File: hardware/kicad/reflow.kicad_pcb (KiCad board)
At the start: 2 copper layers, 104 x 104 mm, 35 parts, among them J1 2 pol skrueterminal, J2 2 pol skrueterminal, J3 MAX31855, J4 OLED, Q1 IRFS4710, Q2 BS170, Q3 BS170, SW1 Rotary 1x12 EYE, SW2 Pushbutton, U2 LM2575-ADJ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

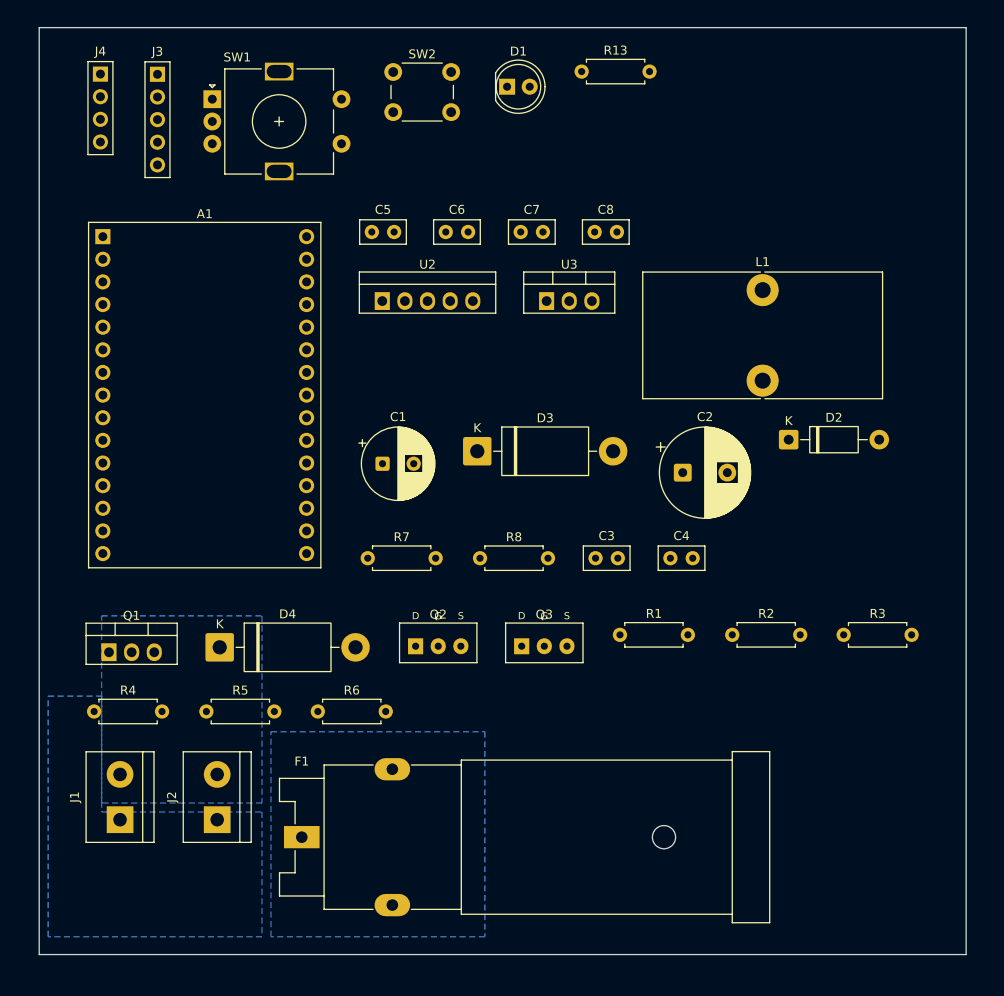
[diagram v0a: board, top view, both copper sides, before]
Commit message: hardware: two-stage route (165 B.Cu tracks + 86 F.Cu jumper segs); 4 connections need manual finish
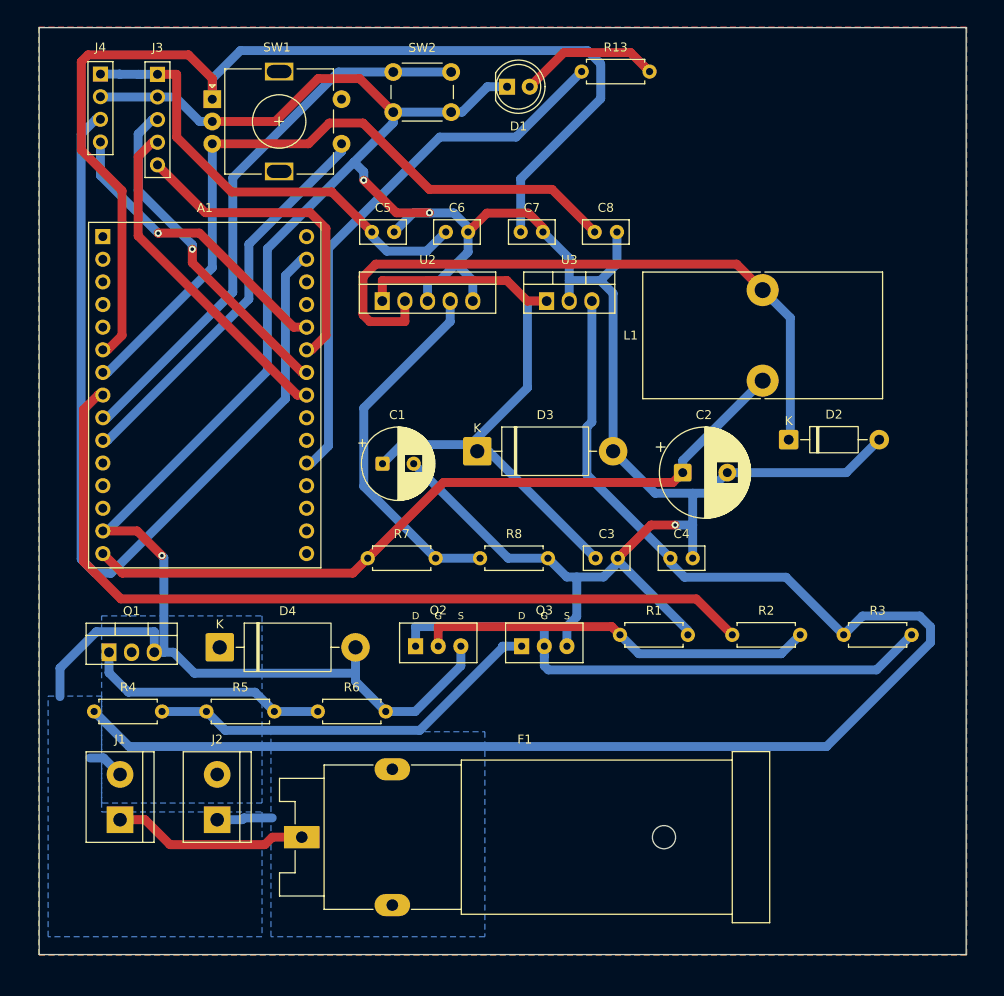
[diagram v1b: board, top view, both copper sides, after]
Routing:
- net /GND: track 0.00 -> 384.5 mm, vias 0 -> 4
- net /+12V: track 0.00 -> 169.5 mm
- net /GPIO32: track 0.00 -> 124.2 mm
- net /GPIO22: track 0.00 -> 99.2 mm
- net /GPIO25: track 0.00 -> 96.1 mm
- net /+5V: track 0.00 -> 84.7 mm
- net /GPIO33: track 0.00 -> 80.0 mm
- net /+24V: track 0.00 -> 78.9 mm
- net /SW_OUT: track 0.00 -> 76.4 mm
- net /GD_NODE1: track 0.00 -> 64.1 mm
- net /GPIO26: track 0.00 -> 62.7 mm
- net /GPIO4: track 0.00 -> 62.0 mm
- net /+3V3: track 0.00 -> 52.3 mm
- net /GATE_MAIN: track 0.00 -> 45.2 mm
- net /Q2_GATE: track 0.00 -> 44.9 mm
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- added copper zone on B.Cu, net (none)
- added copper zone on F.Cu, net (none)
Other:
- board text added: "A1"
- board text added: "C1"
- board text added: "C2"
- board text added: "C3"
- board text added: "C4"
- board text added: "C5"
- board text added: "C6"
- board text added: "C7"
- board text added: "C8"
- board text added: "D1"
- board text added: "D2"
- board text added: "D3"
- board text added: "D4"
- board text added: "F1"
- board text added: "J1"
- board text added: "J2"
- board text added: "J3"
- board text added: "J4"
- board text added: "L1"
- board text added: "Q1"
- board text added: "Q2"
- board text added: "Q3"
- board text added: "R1"
- board text added: "R13"
- board text added: "R2"
- board text added: "R3"
- board text added: "R4"
- board text added: "R5"
- board text added: "R6"
- board text added: "R7"
- board text added: "R8"
- board text added: "SW1"
- board text added: "SW2"
- board text added: "U2"
- board text added: "U3"

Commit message: hardware: close +3V3 on B.Cu; +24V/HEATER_RET need wire bridges
Route A1.30 (/+3V3) to the +3V3 net with a 6-segment B.Cu track down the
clear lane between the ESP module pin column and the buck input, landing on
the existing +3V3 copper. Refill zones. DRC: 0 copper-rule violations, +3V3
connected.

The two high-current crossings (+24V buck-input rail to its pour/F1.2, and
HEATER_RET upper pads to the lower pour island) cannot be closed on the
single-sided B.Cu copper: exhaustive search finds no path at the 1.0 mm
minimum track and no fillable pour neck down to 0.3 mm, because the
buck/gate-drive band plus the full-width +12V track form a continuous
clearance fence. They are left for a manual top-side wire bridge sized for
13 A (HEATER_RET clears at 2.0 mm; +24V at 1.0 mm or with a small
re-placement), rather than forcing a thin power jumper.

Pours intact; board still single-sided (no new B.Cu/F.Cu copper).
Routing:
- net /+3V3: track 52.3 -> 93.0 mm
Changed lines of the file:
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@@
+	)
+	(segment
+		(start 56 45.08)
+		(end 60.5 45.08)
+		(width 1)
+		(layer "B.Cu")
+		(net "/+3V3")
 	)
 	(segment
@@
 	)
 	(segment
+		(start 54.5 66)
+		(end 54.5 54.5)
+		(width 1)
+		(layer "B.Cu")
+		(net "/+3V3")
+	)
+	(segment
+		(start 54.5 54.5)
+		(end 54.5 46)
+		(width 1)
+		(layer "B.Cu")
+		(net "/+3V3")
+	)
+	(segment
 		(start 57.32 43.4026)
 		(end 57.32 42.93)
+		(width 1)
+		(layer "B.Cu")
+		(net "/+3V3")
+	)
+	(segment
+		(start 52 78)
+		(end 54.5 66)
 		(width 1)
 		(layer "B.Cu")
@@
 		(width 1)
 		(layer "B.Cu")
+		(net "/+3V3")
+	)
+	(segment
+		(start 54.5 46)
+		(end 56 45.08)
+		(width 1)
+		(layer "B.Cu")
+		(net "/+3V3")
+	)
+	(segment
+		(start 50 79.01)
+		(end 52 78)
+		(width 1)
+		(layer "B.Cu")

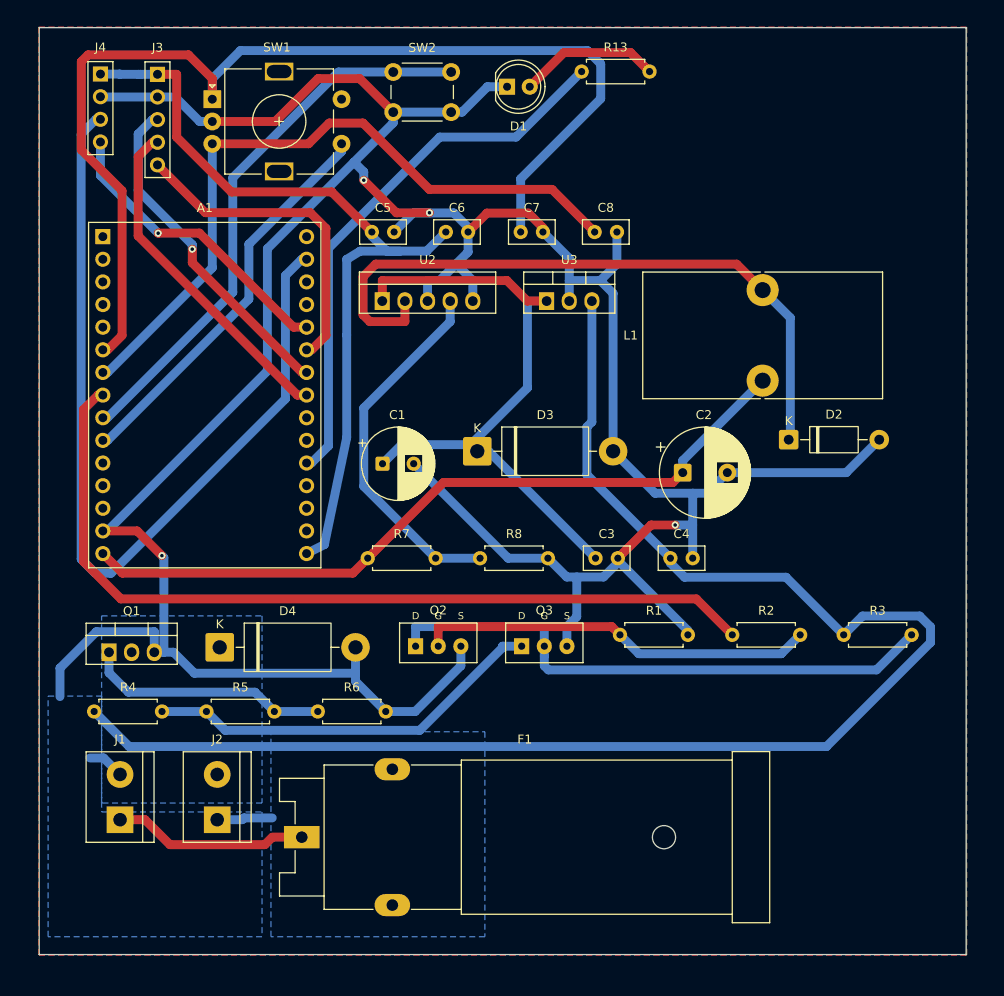
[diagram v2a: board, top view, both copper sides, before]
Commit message: hardware: update board with re-placed footprints (user re-placement)
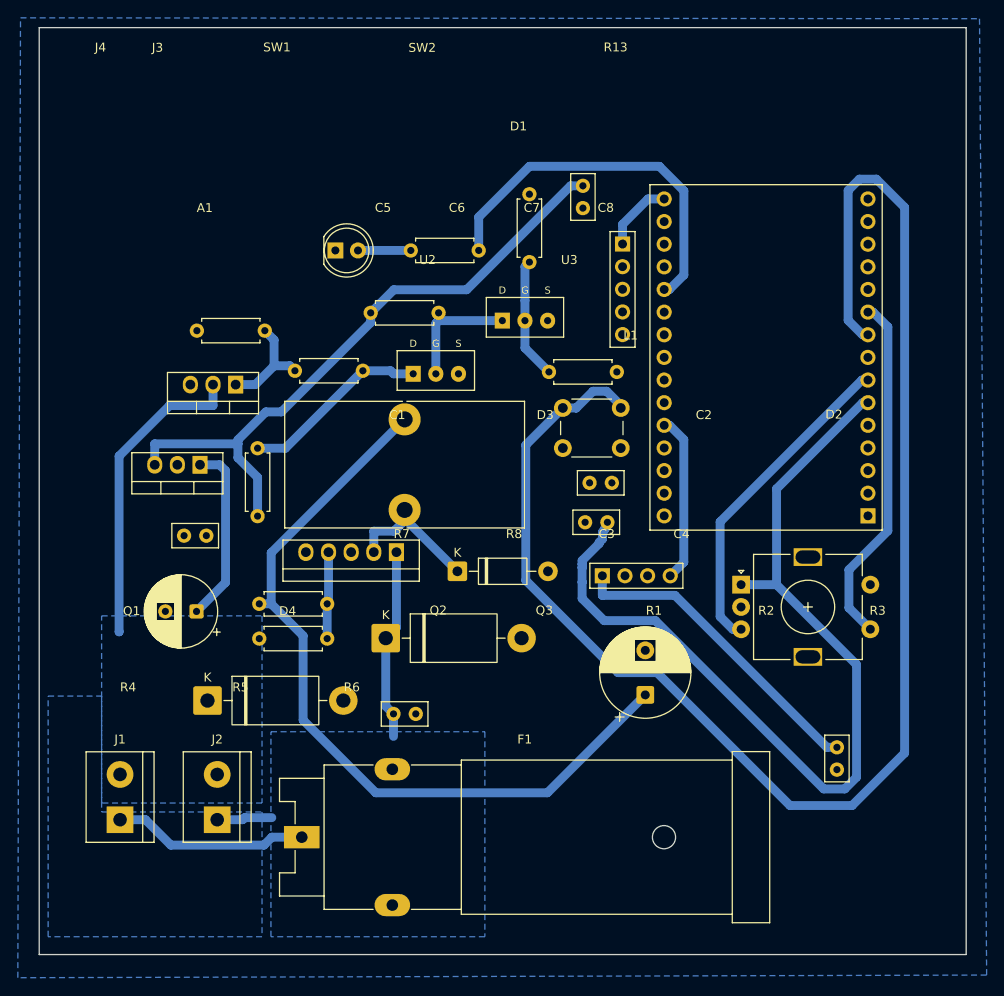
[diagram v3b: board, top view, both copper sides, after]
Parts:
- moved A1 91.4 mm to (113.0, 74.8), turned to 180 degrees
- moved SW1 80.5 mm to (98.8, 82.5)
- moved J4 79.6 mm to (83.2, 81.5), turned to 90 degrees
- moved C5 77.9 mm to (109.5, 100.8), turned to -90 degrees
- moved R3 64.2 mm to (57.2, 52.0)
- moved J3 55.5 mm to (85.5, 44.3)
- moved L1 47.1 mm to (61.0, 74.1), turned to 180 degrees
- moved C6 43.4 mm to (38.8, 77.0), turned to 180 degrees
- moved R6 43.1 mm to (45.3, 54.0), turned to 180 degrees
- moved R1 43.0 mm to (75.0, 46.3), turned to 90 degrees
- moved U3 43.0 mm to (38.0, 69.0), turned to 180 degrees
- moved C4 42.9 mm to (81.0, 37.8), turned to -90 degrees
- moved SW2 42.2 mm to (78.8, 62.7)
- moved R5 42.1 mm to (56.3, 58.5), turned to 180 degrees
- moved D2 40.0 mm to (66.9, 81.0)
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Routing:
- net /GND: track 384.5 -> 0.00 mm, vias 4 -> 0
- net /GPIO26: track 62.7 -> 171.6 mm
- net /GPIO22: track 99.2 -> 0.00 mm
- net /+12V: track 169.5 -> 72.3 mm
- net /GPIO25: track 96.1 -> 0.00 mm
- net /SW_OUT: track 76.4 -> 15.8 mm
- net /GD_NODE1: track 64.1 -> 14.1 mm
- net /+3V3: track 93.0 -> 43.6 mm
- net /GPIO33: track 80.0 -> 36.7 mm
- net /GPIO5: track 38.0 -> 0.00 mm
- net /GPIO18: track 37.7 -> 0.00 mm, vias 1 -> 0
- net /GPIO19: track 36.7 -> 0.00 mm
- net /HEATER_RET: track 0.00 -> 35.0 mm
- net /VFB: track 41.2 -> 9.76 mm
- net /Q2_GATE: track 44.9 -> 13.6 mm
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- removed copper zone on B.Cu, net (none)
- removed copper zone on F.Cu, net (none)
